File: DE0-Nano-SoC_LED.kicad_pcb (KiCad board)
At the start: 2 copper layers, 96.8 x 168.7 mm, 126 parts, among them J1 Conn_02x08_Odd_Even, J10 Conn_01x08, J11 Conn_01x01, J12 Conn_01x01, J13 Conn_01x01, J14 Conn_01x01, J15 Conn_01x01, J16 Conn_01x10, J17 Conn_01x08, J18 Conn_01x01, J19 Conn_01x01, J2 Conn_02x08_Odd_Even, J20 Conn_02x08_Odd_Even, J21 Conn_02x08_Odd_Even, J22 Conn_02x08_Odd_Even, J23 Conn_02x08_Odd_Even, J24 Conn_02x08_Odd_Even, J3 Conn_02x20_Odd_Even, J4 Conn_02x20_Odd_Even, J5 Conn_02x08_Odd_Even, J6 Conn_02x08_Odd_Even, J7 Conn_02x08_Odd_Even, J8 Conn_01x01, J9 Conn_01x06, U1 74HC245, U10 74HC245, U11 74HC245, U12 74HC245, U13 74HC245, U14 74HC245, U15 74HC245, U16 74HC245, U17 74HC245, U18 74HC245, U19 74HC245, U2 74HC245, U20 74HC245, U3 74HC245, U4 74HC245, U5 74HC245, U6 74HC245, U7 74HC245, U8 74HC245, U9 74HC245

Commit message: pcb almost done
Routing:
- net GND: track 327.3 -> 748.9 mm, vias 196 -> 383
- net VCC: track 99.3 -> 109.0 mm, vias 79 -> 86

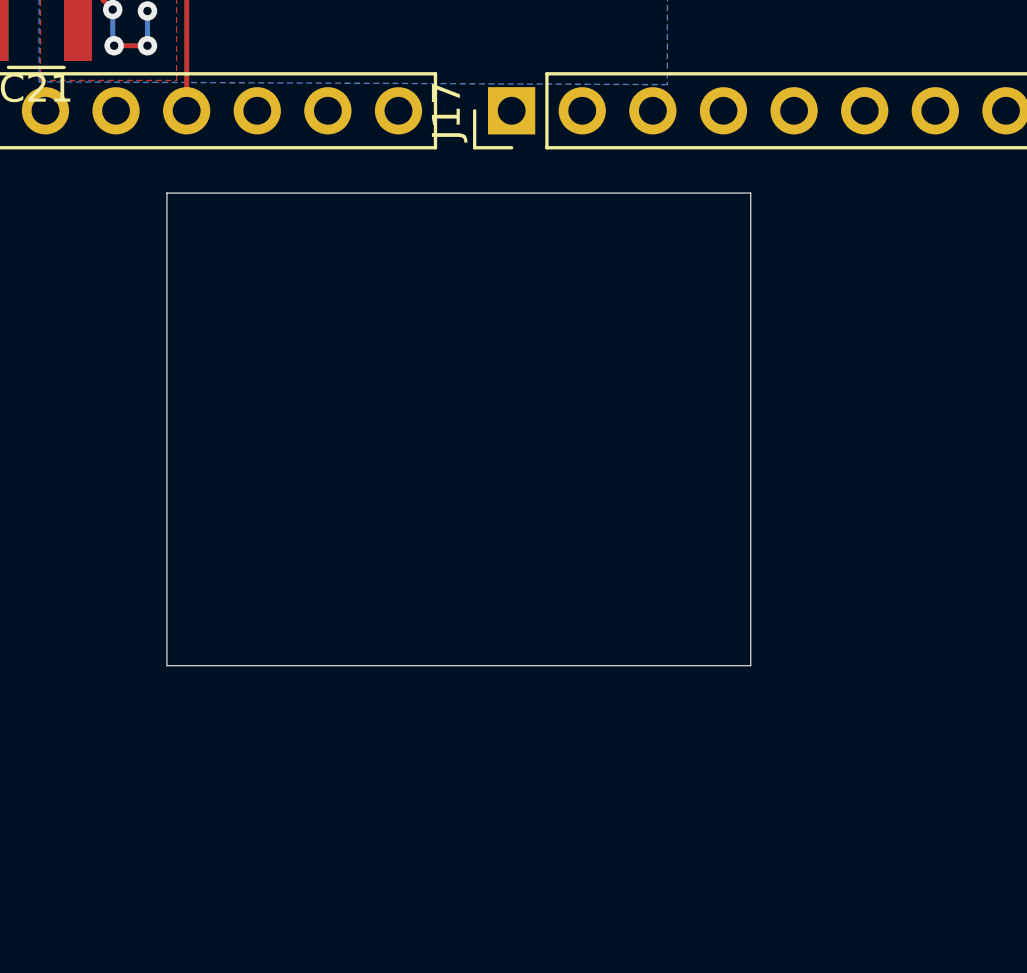
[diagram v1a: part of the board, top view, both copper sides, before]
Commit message: small change in pcb
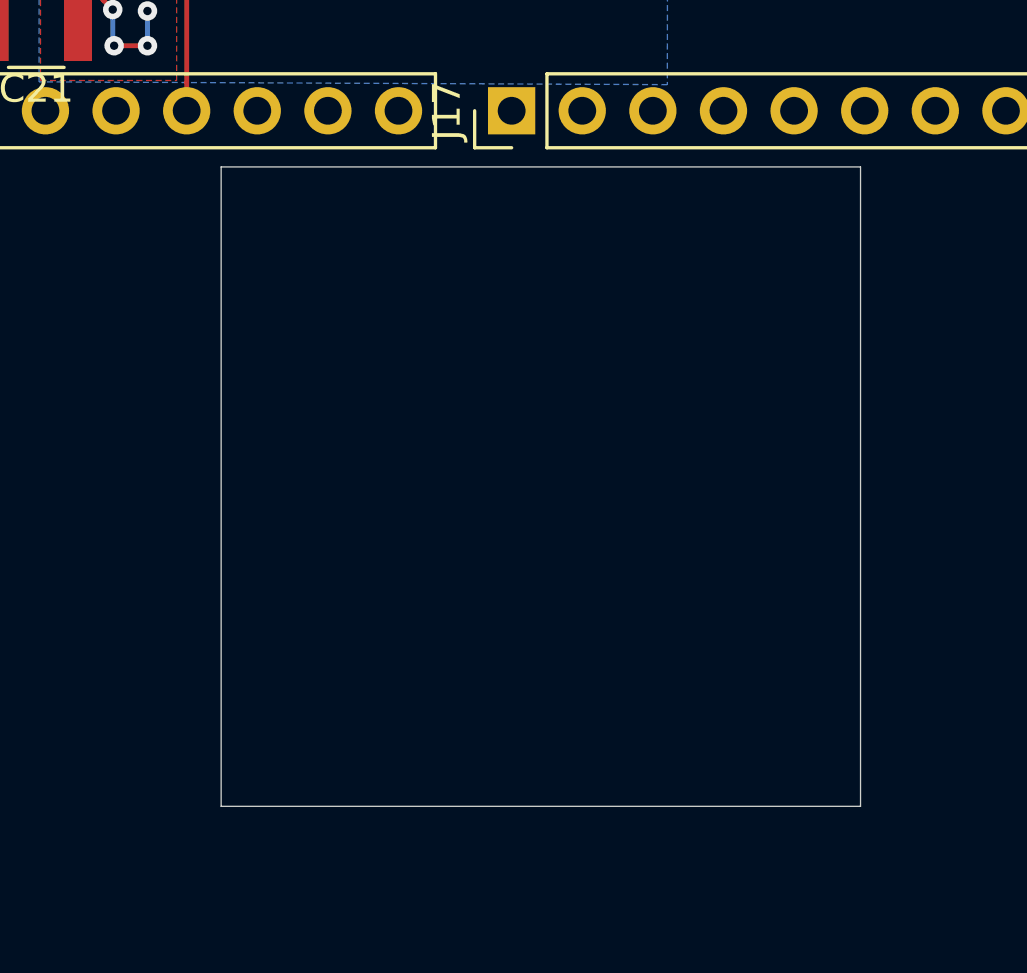
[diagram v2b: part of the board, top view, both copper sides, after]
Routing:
- net GND: vias 383 -> 382
- net (no net): vias 0 -> 1
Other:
- outline, holes or cut-outs redrawn
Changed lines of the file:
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@@
     (arrow2b (pts (xy 66.42 5.63) (xy 67.546504 5.043579)))
   )
-  (gr_line (start 95.05 96.94) (end 95.05 79.94) (layer Edge.Cuts) (width 0.01))
-  (gr_line (start 116.05 96.94) (end 95.05 96.94) (layer Edge.Cuts) (width 0.01))
-  (gr_line (start 116.05 79.94) (end 116.05 96.94) (layer Edge.Cuts) (width 0.01))
-  (gr_line (start 95.05 79.94) (end 116.05 79.94) (layer Edge.Cuts) (width 0.01))
+  (gr_line (start 97 102) (end 97 79) (layer Edge.Cuts) (width 0.01))
+  (gr_line (start 120 102) (end 97 102) (layer Edge.Cuts) (width 0.01))
+  (gr_line (start 120 79) (end 120 102) (layer Edge.Cuts) (width 0.01))
+  (gr_line (start 97 79) (end 120 79) (layer Edge.Cuts) (width 0.01))
   (gr_line (start 67.425 40.34) (end 146.125 40.34) (angle 90) (layer Eco2.User) (width 0.05))
   (gr_line (start 72 44.9) (end 142 44.9) (angle 90) (layer Eco2.User) (width 0.1))
@@
     (arrow2b (pts (xy 70 59.83) (xy 71.126504 59.243579)))
   )
+  (via (at 67.45 137.94) (size 0.7) (drill 0.3) (layers F.Cu B.Cu) (net 0))
   (via (at 67.45 177.94) (size 0.7) (drill 0.3) (layers F.Cu B.Cu) (net 1))
   (via (at 67.45 175.94) (size 0.7) (drill 0.3) (layers F.Cu B.Cu) (net 1))
@@
   (via (at 67.45 141.94) (size 0.7) (drill 0.3) (layers F.Cu B.Cu) (net 1))
   (via (at 67.45 139.94) (size 0.7) (drill 0.3) (layers F.Cu B.Cu) (net 1))
-  (via (at 67.45 137.94) (size 0.7) (drill 0.3) (layers F.Cu B.Cu) (net 1))
   (via (at 67.45 135.94) (size 0.7) (drill 0.3) (layers F.Cu B.Cu) (net 1))
   (via (at 67.45 127.94) (size 0.7) (drill 0.3) (layers F.Cu B.Cu) (net 1))

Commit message: silk and logo added, gerber generated
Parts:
- added G***: LOGO, logos:LOGO, F.Cu at (114.0, 114.3)
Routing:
- net GND: track 748.9 -> 841.9 mm, vias 382 -> 429
- net (no net): vias 1 -> 0
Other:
- outline, holes or cut-outs redrawn
- board text added: "1"
- board text added: "10"
- board text added: "2"
- board text added: "3"
- board text added: "4"
- board text added: "5"
- board text added: "6"
- board text added: "7"
- board text added: "8"
- board text added: "9"
- board text added: "DE0-Nano-SoC LED fanout v1.0"

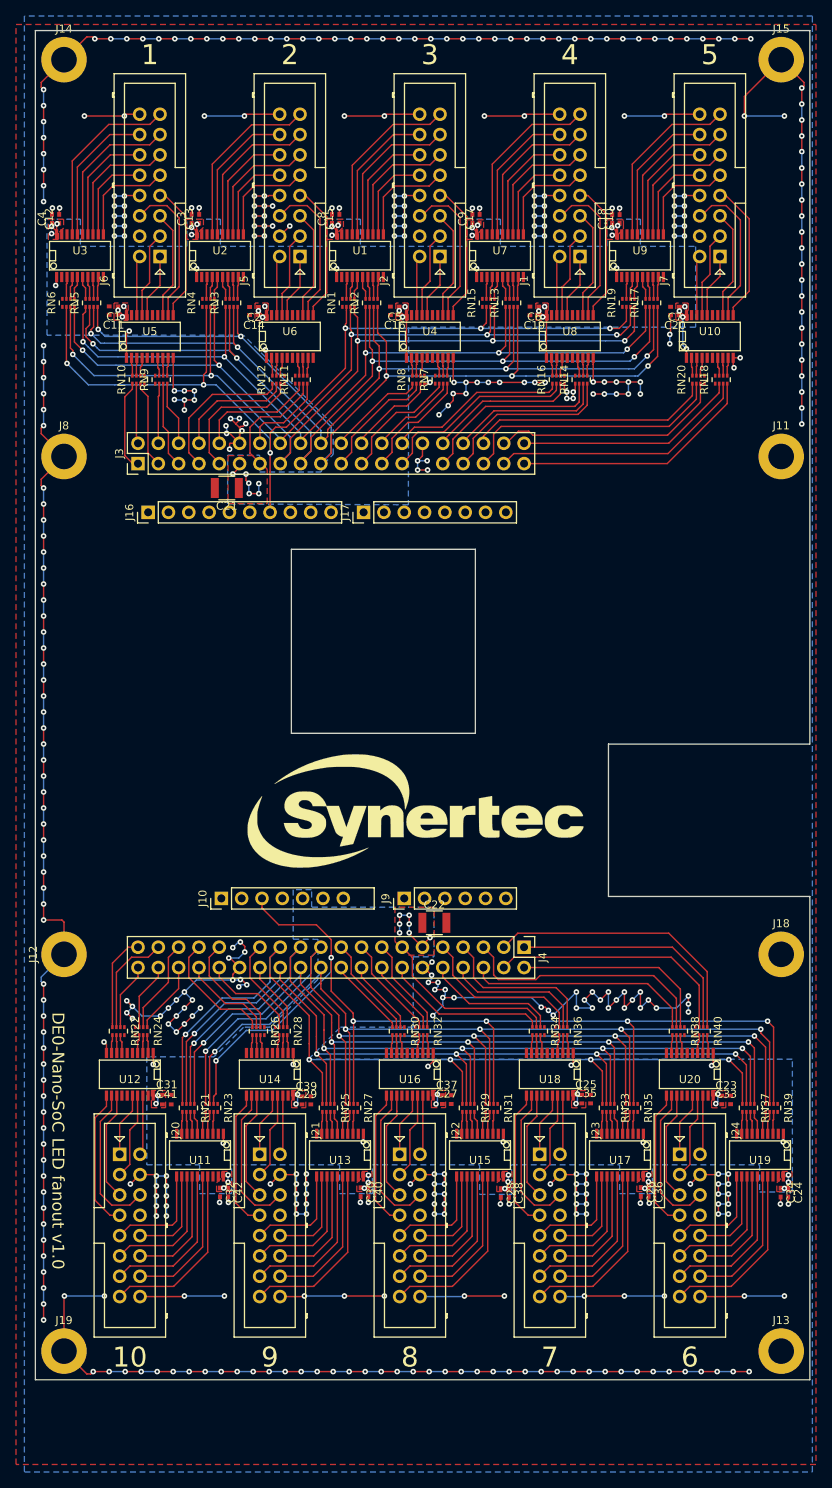
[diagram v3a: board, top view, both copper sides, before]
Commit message: new connectors
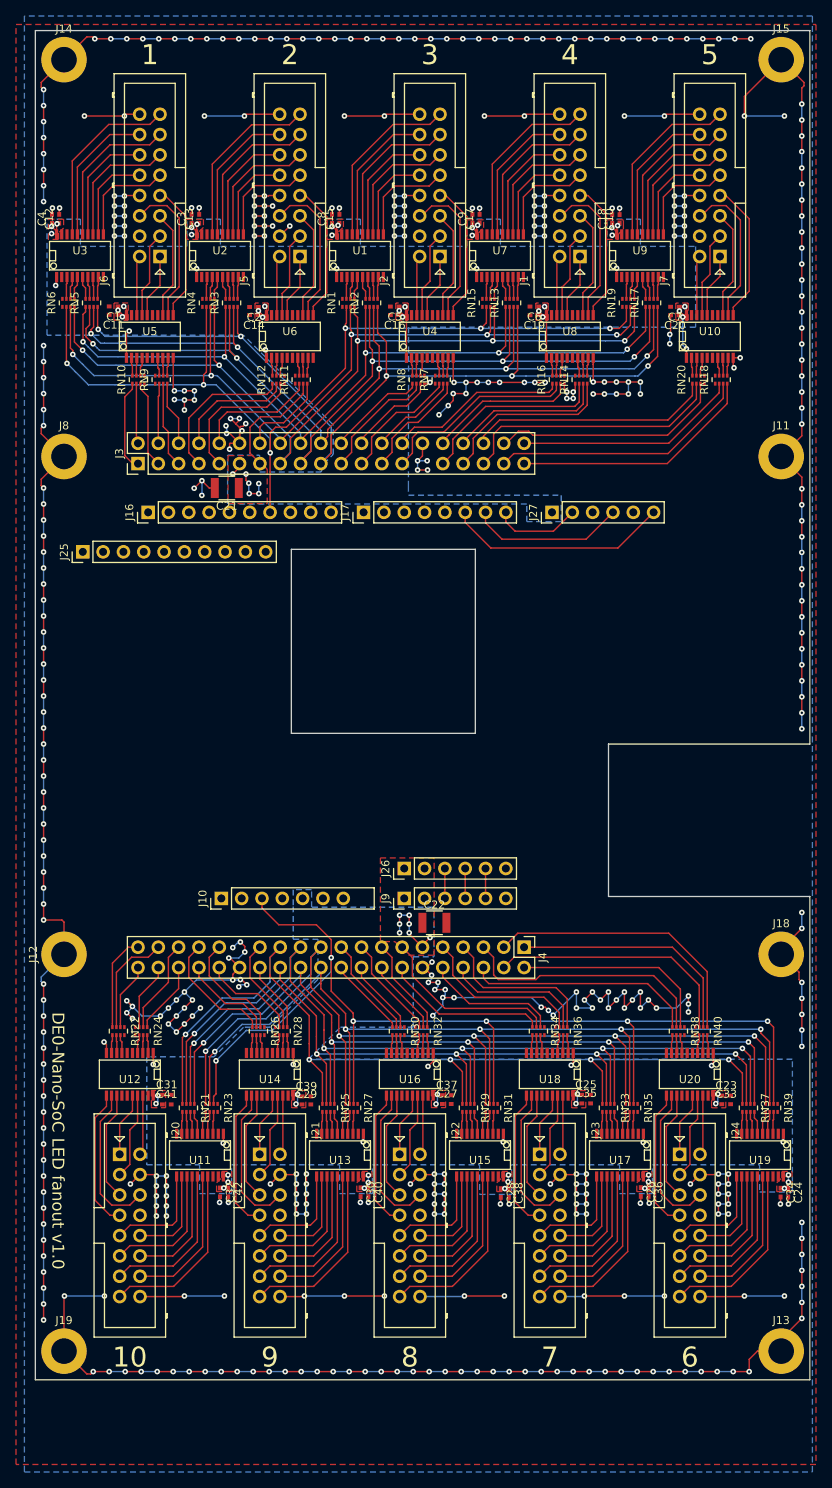
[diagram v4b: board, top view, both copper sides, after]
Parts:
- removed G***: LOGO, logos:LOGO
- added J25: Conn_01x10, Pin_Headers:Pin_Header_Straight_1x10_Pitch2.54mm, F.Cu at (72.3, 81.9)
- added J26: Conn_01x06, Pin_Headers:Pin_Header_Straight_1x06_Pitch2.54mm, F.Cu at (112.5, 121.5)
- added J27: Conn_01x06, Pin_Headers:Pin_Header_Straight_1x06_Pitch2.54mm, F.Cu at (131.0, 77.0)
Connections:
- net Net-(J9-Pad1) renamed /ADC_IN0
- net Net-(J9-Pad2) renamed /ADC_IN1
- net Net-(J9-Pad6) renamed /ADC_IN5
- J17 pad 6: Net-(J17-Pad6) -> /FPGA_AG10
- J17 pad 7: Net-(J17-Pad7) -> /FPGA_AF13
- J17 pad 8: Net-(J17-Pad8) -> /FPGA_AG13
- J9 pad 3: Net-(J9-Pad3) -> /ADC_IN2
- J9 pad 4: Net-(J9-Pad4) -> /ADC_IN3
- J9 pad 5: Net-(J9-Pad5) -> /ADC_IN4
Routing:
- net GND: track 841.9 -> 929.8 mm, vias 429 -> 461
- net /FPGA_AG10: track 0.00 -> 28.0 mm
- net /FPGA_AF13: track 0.00 -> 19.5 mm
- net /FPGA_AG13: track 0.00 -> 11.0 mm
- net /ADC_IN4: track 0.00 -> 3.74 mm
- net /ADC_IN3: track 0.00 -> 3.74 mm
- net /ADC_IN2: track 0.00 -> 3.74 mm

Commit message: what should I add to the board?
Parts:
- added G10: LOGO, logos:LOGO, F.Cu at (113.0, 114.2)
- added J28: Conn_01x10, Pin_Headers:Pin_Header_Straight_1x10_Pitch2.54mm, F.Cu at (72.3, 106.9)
- moved J25 0.05 mm to (72.3, 81.9)
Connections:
- J16 pad 1: Net-(J16-Pad1) -> /FPGA_AG11
- J16 pad 2: Net-(J16-Pad2) -> /FPGA_AH9
- J16 pad 5: Net-(J16-Pad5) -> /FPGA_AH12
- J16 pad 6: Net-(J16-Pad6) -> /FPGA_AH11
- J16 pad 7: /OE__1 -> /FPGA_AG16
- J16 pad 8: Net-(J16-Pad8) -> /OE__1
- J25 pad 1: Net-(J25-Pad1) -> /FPGA_AG11
- J25 pad 10: Net-(J25-Pad10) -> VCC
- J25 pad 2: Net-(J25-Pad2) -> /FPGA_AH9
- J25 pad 3: Net-(J25-Pad3) -> GND
- J25 pad 4: Net-(J25-Pad4) -> GND
- J25 pad 5: Net-(J25-Pad5) -> /FPGA_AH12
- J25 pad 6: Net-(J25-Pad6) -> /FPGA_AH11
- J25 pad 7: Net-(J25-Pad7) -> /FPGA_AG16
- J25 pad 8: Net-(J25-Pad8) -> VCC
- J25 pad 9: Net-(J25-Pad9) -> VCC
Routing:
- net /FPGA_AG11: track 0.00 -> 10.9 mm
- net /FPGA_AH12: track 0.00 -> 10.3 mm
- net /FPGA_AH9: track 0.00 -> 10.3 mm
- net /FPGA_AH11: track 0.00 -> 10.3 mm
- net /FPGA_AG16: track 0.00 -> 10.3 mm
- net /OE__1: track 118.7 -> 119.8 mm
- net GND: track 929.8 -> 930.9 mm, vias 461 -> 462

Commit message: final version of the board
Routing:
- net (no net): track 0.00 -> 5.66 mm, vias 0 -> 3
- net GND: track 930.9 -> 928.6 mm, vias 462 -> 458

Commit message: supa small pcb fix
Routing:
- net (no net): track 5.66 -> 0.00 mm, vias 3 -> 0
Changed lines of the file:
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@@
     (links 717)
     (no_connects 2)
-    (area 66.414999 16.754999 163.235001 185.415001)
+    (area 9.994999 2.93 180.834286 196.940001)
     (thickness 1.6)
     (drawings 67)
-    (tracks 2971)
+    (tracks 2964)
     (zones 0)
     (modules 131)
@@
     (arrow2b (pts (xy 70 59.83) (xy 71.126504 59.243579)))
   )
-  (segment (start 86.05 139.94) (end 87.05 138.94) (width 0.18) (layer B.Cu) (net 0))
-  (via (at 87.05 138.94) (size 0.7) (drill 0.3) (layers F.Cu B.Cu) (net 0))
-  (segment (start 85.05 140.94) (end 86.05 139.94) (width 0.18) (layer F.Cu) (net 0))
-  (segment (start 84.05 141.94) (end 85.05 140.94) (width 0.18) (layer F.Cu) (net 0))
-  (via (at 85.05 140.94) (size 0.7) (drill 0.3) (layers F.Cu B.Cu) (net 0))
-  (segment (start 83.05 140.94) (end 84.05 141.94) (width 0.18) (layer B.Cu) (net 0))
-  (via (at 84.05 141.94) (size 0.7) (drill 0.3) (layers F.Cu B.Cu) (net 0))
   (segment (start 119.55 127.54) (end 119.55 128.84) (width 0.18) (layer B.Cu) (net 1))
   (via (at 119.55 128.84) (size 0.7) (drill 0.3) (layers F.Cu B.Cu) (net 1))

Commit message: silk small fix
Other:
- board text added: "DE0-Nano-SoC LED fanout v1.1"
- board text added: "GND"
- board text added: "GPS RX"
- board text added: "VCC"
- board text removed: "DE0-Nano-SoC LED fanout v1.0"
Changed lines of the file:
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@@
 (kicad_pcb (version 4) (host pcbnew 4.0.7-e2-6376~58~ubuntu16.04.1)
   (general
-    (links 717)
+    (links 0)
     (no_connects 2)
     (area 9.994999 2.93 180.834286 196.940001)
     (thickness 1.6)
-    (drawings 67)
+    (drawings 75)
     (tracks 2964)
     (zones 0)
@@
     (zone_45_only yes)
     (trace_min 0.18)
-    (segment_width 0.2)
+    (segment_width 0.15)
     (edge_width 0.15)
     (via_size 0.7)
@@
     )
   )
-  (gr_text "DE0-Nano-SoC LED fanout v1.0" (at 69.24 155.54 270) (layer F.SilkS)
+  (gr_line (start 132.27 89.94) (end 132.27 75.67) (layer F.SilkS) (width 0.15))
+  (gr_line (start 134.81 89.94) (end 134.81 75.67) (layer F.SilkS) (width 0.15))
+  (gr_line (start 137.35 89.94) (end 137.35 75.67) (layer F.SilkS) (width 0.15))
+  (gr_line (start 129.65 89.94) (end 137.35 89.94) (layer F.SilkS) (width 0.15))
+  (gr_line (start 129.685 78.34) (end 129.685 89.94) (layer F.SilkS) (width 0.15))
+  (gr_text "VCC\n" (at 131 83.6 90) (layer F.SilkS)
+    (effects (font (size 1.3 1.3) (thickness 0.3)))
+  )
+  (gr_text GND (at 136.08 83.7 90) (layer F.SilkS)
+    (effects (font (size 1.3 1.3) (thickness 0.3)))
+  )
+  (gr_text "GPS RX" (at 133.54 85.5 90) (layer F.SilkS)
+    (effects (font (size 1.3 1.3) (thickness 0.3)))
+  )
+  (gr_text "DE0-Nano-SoC LED fanout v1.1" (at 69.24 155.54 270) (layer F.SilkS)
     (effects (font (size 1.3 1.3) (thickness 0.3)))
   )
